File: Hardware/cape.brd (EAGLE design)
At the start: 118.2 x 103.5 mm, 40 parts, among them IC2 74VHC541, IC4 74VHC541, IC5 74VHC541, J1 FCI-10118064-5001310LF, J2 FCI-10118064-5001310LF, J3 RJ45-8P8C, Q2 N-MOSFET-DUALSO8, Q3 N-MOSFET-DUALSO8, Q4 N-MOSFET-DUALSO8, Q5 N-MOSFET-DUALSO8, Q6 N-MOSFET-DUALSO8, Q7 N-MOSFET-DUALSO8, Q8 N-MOSFET-DUALSO8, Q9 N-MOSFET-DUALSO8

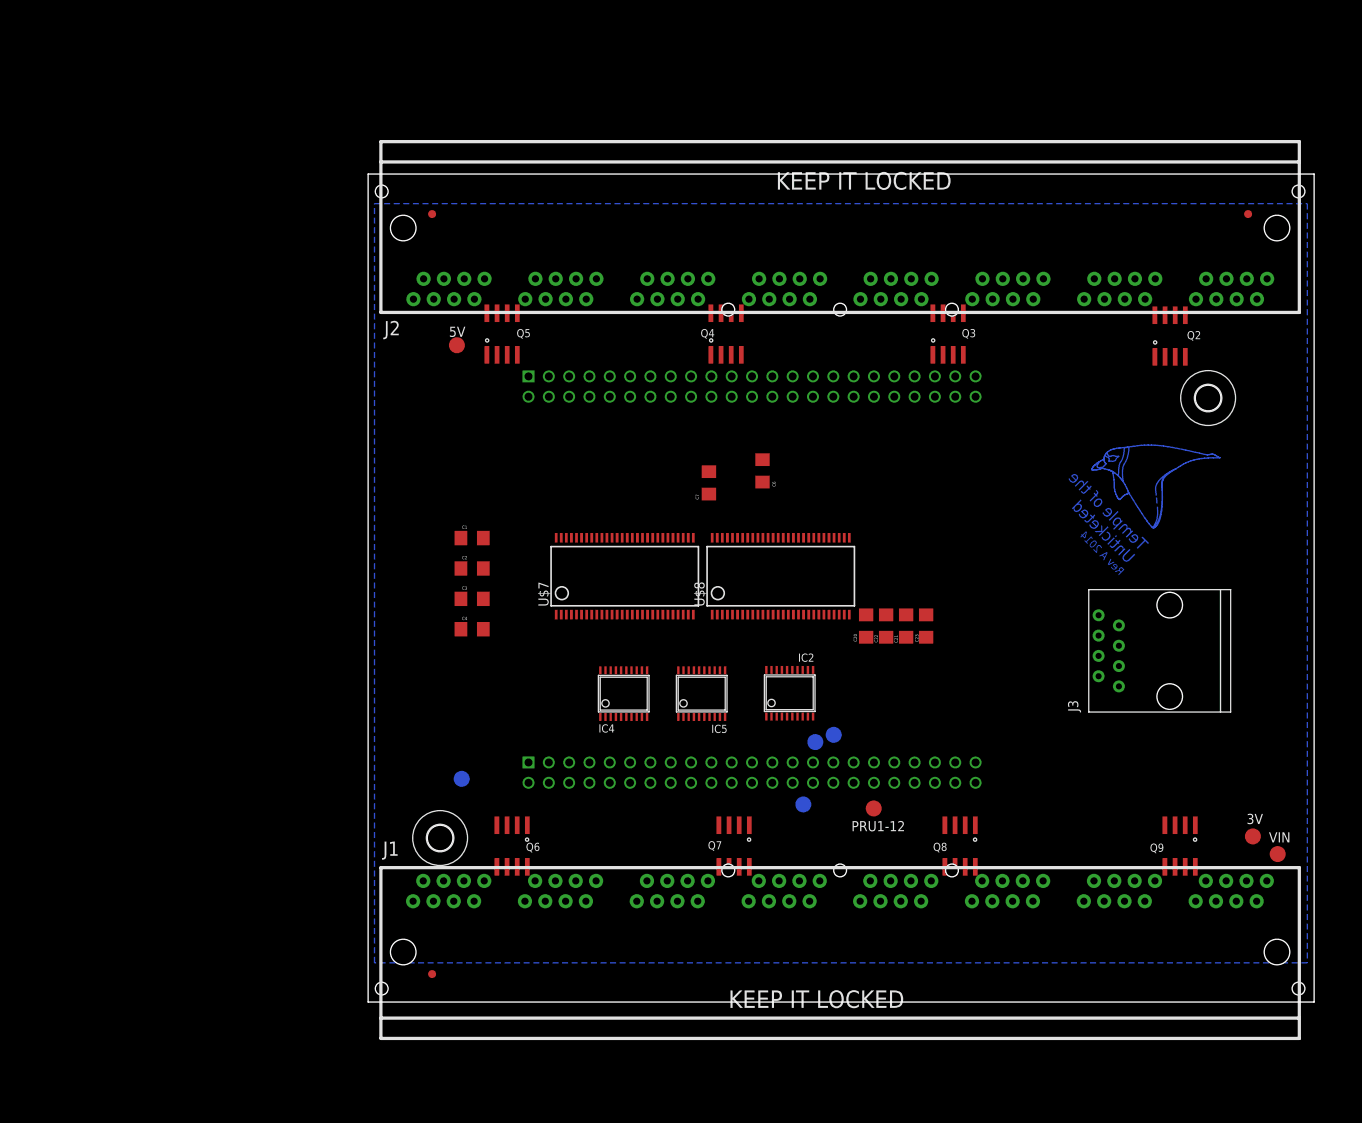
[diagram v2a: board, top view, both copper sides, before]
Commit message: Work on routing A/B and mosfets
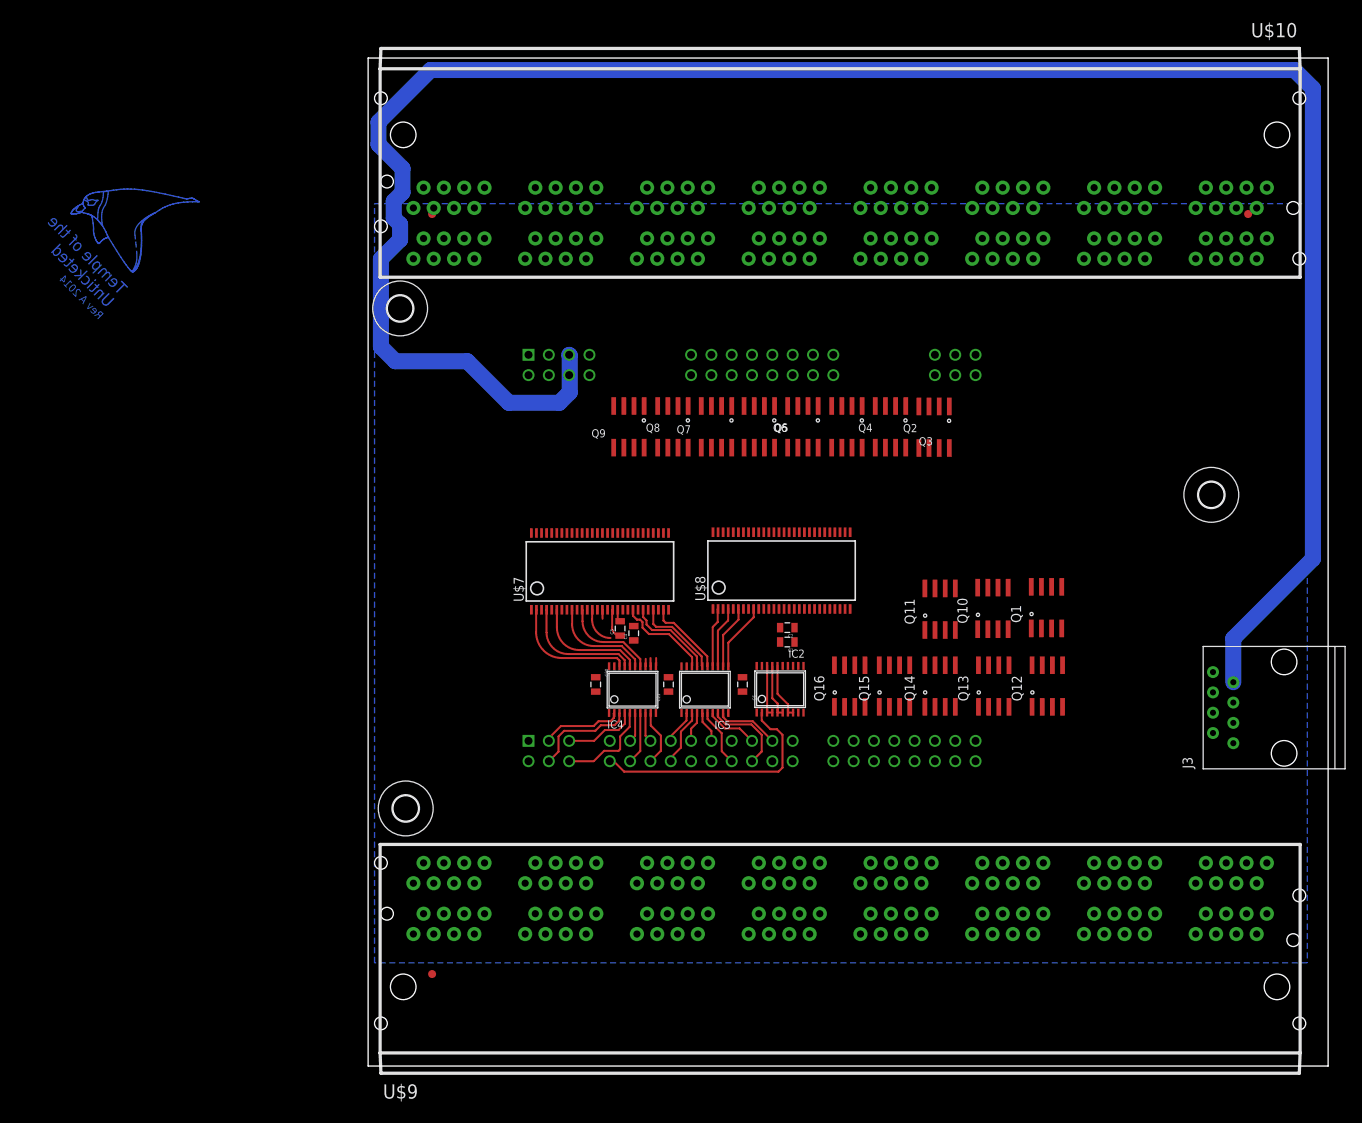
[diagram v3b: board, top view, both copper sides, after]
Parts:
- removed 3V, 5V, GND, PRU1-10, PRU1-12, PRU1-8, PRU1-9, VIN: PTR1TP20R, tenna_avr_AD7021_v0_9_shrink:TP20R
- removed C22, C23, C7: 10uF, SparkFun-Capacitors:1206
- removed J1, J2: FCI-10118064-5001310LF, cape:FCI-10118064-5001310LF
- added Q1, Q10, Q11, Q12, Q13, Q14, Q15, Q16: N-MOSFET-DUALSO8, cape:SO8
- added U$10, U$9: RJ45-8P8C-16FCI-16, cape:FCI-10118074-500A010LF
- added U$12: (no value), holes:3,2
- C1, C2, C20, C21, C3, C4, C6: device SparkFun-Capacitors:1206 -> SparkFun-Capacitors:0805
- moved Q9 86.6 mm to (32.6, 71.9)
- moved Q8 63.5 mm to (38.1, 71.9)
- moved Q6 60.8 mm to (48.9, 71.9)
- moved Q7 52.4 mm to (43.5, 71.9)
- moved C1 41.5 mm to (52.4, 45.0), turned to 180 degrees
- moved C2 40.1 mm to (52.4, 46.8), turned to 180 degrees
- moved Q5 39.3 mm to (54.4, 71.9), turned to 180 degrees
- moved C20 34.6 mm to (28.4, 39.7), turned to 270 degrees
- moved Q2 31.6 mm to (70.8, 71.8), turned to 180 degrees
- moved C21 30.6 mm to (37.5, 39.7)
- moved C6 26.8 mm to (46.8, 39.7)
- moved C4 20.2 mm to (33.2, 46.1), turned to 90 degrees
- moved Q4 19.0 mm to (59.9, 71.9), turned to 180 degrees
- moved C3 18.9 mm to (31.5, 46.7), turned to 90 degrees
- moved J3 16.0 mm to (114.5, 36.8)
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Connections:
- removed net AIN0: U$1.85
- removed net BL0: J1.A6
- removed net BL1: J1.B6
- removed net BL10: J2.C6
- removed net BL11: J2.D6
- removed net BL12: J2.E6
- removed net BL13: J2.F6
- removed net BL14: J2.G6
- removed net BL15: J2.H6
- removed net BL2: J1.C6
- removed net BL3: J1.D6
- removed net BL4: J1.E6
- removed net BL5: J1.F6
- removed net BL6: J1.G6
- removed net BL7: J1.H6
- removed net BL8: J2.A6
- removed net BL9: J2.B6
- removed net DATA0: J1.A1
- removed net DATA1: J1.B1
- removed net DATA10: J2.C1
- removed net DATA11: J2.D1
- removed net DATA12: J2.E1
- removed net DATA13: J2.F1
- removed net DATA14: J2.G1
- removed net DATA15: J2.H1
- removed net DATA2: J1.C1
- removed net DATA3: J1.D1
- removed net DATA4: J1.E1
- removed net DATA5: J1.F1
- removed net DATA6: J1.G1
- removed net DATA7: J1.H1
- removed net DATA8: J2.A1
- removed net DATA9: J2.B1
- removed net DC0: J1.A4, J1.B4, J1.C4, J1.D4
- removed net DC1: J1.E4, J1.F4, J1.G4, J1.H4
- removed net DC2: J2.A4, J2.B4, J2.C4, J2.D4
- removed net DC3: J2.E4, J2.F4, J2.G4, J2.H4
- removed net N$1: Q6.7, Q6.8
- removed net N$2: Q6.5, Q6.6
- removed net N$29: Q9.7, Q9.8
- removed net N$3: Q7.7, Q7.8
- removed net N$30: Q9.5, Q9.6
- removed net N$31: Q2.7, Q2.8
- removed net N$34: Q2.5, Q2.6
- removed net N$35: Q3.7, Q3.8
- removed net N$36: Q3.5, Q3.6
- removed net N$37: Q4.7, Q4.8
- removed net N$38: Q4.5, Q4.6
- removed net N$39: Q5.7, Q5.8
- removed net N$4: Q7.5, Q7.6
- removed net N$40: Q5.5, Q5.6
- removed net N$7: Q8.7, Q8.8
- removed net N$8: Q8.5, Q8.6
- removed net PRU0-0: Q2.2, U$1.77
- removed net PRU0-1: Q2.4, U$1.75
- removed net PRU0-2: Q3.2, U$1.76
- removed net PRU0-3: Q3.4, U$1.74
- removed net PRU0-4: Q4.2, U$1.88
- removed net PRU0-5: Q4.4, U$1.73
- removed net PRU0-6: Q5.2, U$1.87
- removed net PRU0-7: Q5.4, U$1.71
- removed net PRU1-0: Q6.2, U$1.45
- removed net PRU1-1: Q6.4, U$1.46
- removed net PRU1-10: PRU1-10.TP, U$1.28
- removed net PRU1-12: PRU1-12.TP, U$1.21
- removed net PRU1-2: Q7.2, U$1.43
- removed net PRU1-3: Q7.4, U$1.44
- removed net PRU1-4: Q8.2, U$1.41
- removed net PRU1-5: Q8.4, U$1.42
- removed net PRU1-6: Q9.2, U$1.39
- removed net PRU1-7: Q9.4, U$1.40
- removed net PRU1-8: PRU1-8.TP, U$1.27
- removed net PRU1-9: PRU1-9.TP, U$1.29
- removed net SCK0: J1.A8, J1.B8, J1.C8, J1.D8
- removed net SCK1: J1.E8, J1.F8, J1.G8, J1.H8
- removed net SCK2: J2.A8, J2.B8, J2.C8, J2.D8
- removed net SCK3: J2.E8, J2.F8, J2.G8, J2.H8
- removed net VIN: VIN.TP
- new net BL-0-1: Q2.7, Q2.8, U$10.UA6
- new net BL-0-2: Q2.5, Q2.6, U$10.LA6
- new net BL-1-1: Q3.7, Q3.8, U$10.UB6
- new net BL-1-2: Q3.5, Q3.6, U$10.LB6
- new net BL-10-1: U$9.LH6
- new net BL-10-2: U$9.UH6
- new net BL-11-1: Q7.7, Q7.8, U$10.UF6
- new net BL-11-2: Q7.5, Q7.6, U$10.LF6
- new net BL-12-2: U$9.UF6
- new net BL-13-1: U$9.LE6
- new net BL-13-2: U$9.UE6
- new net BL-14-1: Q8.7, Q8.8, U$10.UG6
- new net BL-14-2: Q8.5, Q8.6, U$10.LG6
- new net BL-15-1: Q9.7, Q9.8, U$10.UH6
- new net BL-15-2: Q9.5, Q9.6, U$10.LH6
- new net BL-2-1: U$9.LC6
- new net BL-2-2: U$9.UC6
- new net BL-3-1: U$9.LD6
- new net BL-3-2: U$9.UD6
- new net BL-4-1: Q4.7, Q4.8, U$10.UC6
- new net BL-4-2: Q4.5, Q4.6, U$10.LC6
- new net BL-5-1: Q5.7, Q5.8, U$10.UD6
- new net BL-5-2: Q5.5, Q5.6, U$10.LD6
- new net BL-6-1: U$9.LA6
- new net BL-6-2: U$9.UA6
- new net BL-7-1: U$9.LB6
- new net BL-7-2: U$9.UB6
- new net BL-8-1: Q6.7, Q6.8, U$10.UE6
- new net BL-8-2: Q6.5, Q6.6, U$10.LE6
- new net BL-9-1: U$9.LG6
- new net BL-9-2: U$9.UG6
- new net DATA-0-1: U$10.UA1, U$8.47
- new net DATA-0-2: U$10.LA1, U$8.46
- new net DATA-1-1: U$10.UB1, U$8.50
- new net DATA-1-2: U$10.LB1, U$8.48
- new net DATA-10-1: U$7.39, U$9.LH1
- new net DATA-10-2: U$7.37, U$9.UH1
- new net DATA-11-1: U$10.UF1, U$7.32
- new net DATA-11-2: U$10.LF1, U$7.31
- new net DATA-12-1: U$7.43, U$9.LF1
- new net DATA-12-2: U$7.42, U$9.UF1
- new net DATA-13-1: U$7.45, U$9.LE1
- new net DATA-13-2: U$7.44, U$9.UE1
- new net DATA-14-1: U$10.UG1, U$7.34
- new net DATA-14-2: U$10.LG1, U$7.33
- new net DATA-15-1: U$10.UH1, U$7.36
- new net DATA-15-2: U$10.LH1, U$7.35
- new net DATA-2-1: U$7.50, U$9.LC1
- new net DATA-2-2: U$7.48, U$9.UC1
- new net DATA-3-1: U$7.47, U$9.LD1
- new net DATA-3-2: U$7.46, U$9.UD1
- new net DATA-4-1: U$10.UC1, U$8.52
- new net DATA-4-2: U$10.LC1, U$8.51
- new net DATA-5-1: U$10.UD1, U$8.54
- new net DATA-5-2: U$10.LD1, U$8.53
- new net DATA-6-1: U$7.54, U$9.LA1
- new net DATA-6-2: U$7.53, U$9.UA1
- new net DATA-7-1: U$7.52, U$9.LB1
- new net DATA-7-2: U$7.51, U$9.UB1
- new net DATA-8-1: U$10.UE1, U$7.30
- new net DATA-8-2: U$10.LE1, U$7.29
- new net DATA-9-1: U$7.41, U$9.LG1
- new net DATA-9-2: U$7.40, U$9.UG1
- new net DC: U$10.LA4, U$10.LB4, U$10.LC4, U$10.LD4, U$10.LE4, U$10.LF4, U$10.LG4, U$10.LH4, U$10.UA4, U$10.UB4, U$10.UC4, U$10.UD4, U$10.UE4, U$10.UF4, U$10.UG4, U$10.UH4, U$9.LA4, U$9.LB4, U$9.LC4, U$9.LD4, U$9.LE4, U$9.LF4, U$9.LG4, U$9.LH4, U$9.UA4, U$9.UB4, U$9.UC4, U$9.UD4, U$9.UE4, U$9.UF4, U$9.UG4, U$9.UH4
- new net MUX_S: U$1.28, U$7.1, U$8.1
- new net N$10: Q14.5, Q14.6
- new net N$11: Q15.7, Q15.8
- new net N$12: Q15.5, Q15.6
- new net N$13: Q16.7, Q16.8
- new net N$14: Q16.5, Q16.6
- new net N$15: Q1.7, Q1.8
- new net N$16: Q1.5, Q1.6
- new net N$17: Q10.7, Q10.8
- new net N$18: Q10.5, Q10.6
- new net N$19: Q11.7, Q11.8
- new net N$20: Q11.5, Q11.6
- new net N$21: Q12.7, Q12.8
- new net N$22: U$9.LF6
- new net N$23: Q12.5, Q12.6
- new net N$5: Q13.7, Q13.8
- new net N$6: Q13.5, Q13.6
- new net N$9: Q14.7, Q14.8
- new net PWM0: Q2.2, U$1.87
- new net PWM1: Q2.4, U$1.88
- new net PWM10: Q7.2, U$1.69
- new net PWM11: Q7.4, U$1.68
- new net PWM12: Q8.2, U$1.67
- new net PWM13: Q8.4, U$1.66
- new net PWM14: Q9.2, U$1.65
- new net PWM15: Q9.4, U$1.64
- new net PWM16: Q1.2, U$1.45
- new net PWM17: Q1.4, U$1.46
- new net PWM18: Q10.2, U$1.43
- new net PWM19: Q10.4, U$1.44
- new net PWM2: Q3.2, U$1.77
- new net PWM20: Q11.2, U$1.41
- new net PWM21: Q11.4, U$1.42
- new net PWM22: Q12.2, U$1.39
- new net PWM23: Q12.4, U$1.40
- new net PWM24: Q13.2, U$1.37
- new net PWM25: Q13.4, U$1.38
- new net PWM26: Q14.2, U$1.35
- new net PWM27: Q14.4, U$1.36
- new net PWM28: Q15.2, U$1.33
- new net PWM29: Q15.4, U$1.34
- new net PWM3: Q3.4, U$1.76
- new net PWM30: Q16.2, U$1.31
- new net PWM31: Q16.4, U$1.32
- new net PWM4: Q4.2, U$1.75
- new net PWM5: Q4.4, U$1.74
- new net PWM6: Q5.2, U$1.73
- new net PWM7: Q5.4, U$1.72
- new net PWM8: Q6.2, U$1.71
- new net PWM9: Q6.4, U$1.70
- new net SCL-A-1: U$8.45, U$9.LA8, U$9.LB8
- new net SCL-A-2: U$8.44, U$9.UA8, U$9.UB8
- new net SCL-B-1: U$8.43, U$9.LC8, U$9.LD8
- new net SCL-B-2: U$8.42, U$9.UC8, U$9.UD8
- new net SCL-C-1: U$8.41, U$9.LE8, U$9.LF8
- new net SCL-C-2: U$8.40, U$9.UE8, U$9.UF8
- new net SCL-D-1: U$8.39, U$9.LG8, U$9.LH8
- new net SCL-D-2: U$8.37, U$9.UG8, U$9.UH8
- new net SCL-E-1: U$10.UG8, U$10.UH8, U$8.36
- new net SCL-E-2: U$10.LG8, U$10.LH8, U$8.35
- new net SCL-F-1: U$10.UE8, U$10.UF8, U$8.34
- new net SCL-F-2: U$10.LE8, U$10.LF8, U$8.33
- new net SCL-G-1: U$10.UC8, U$10.UD8, U$8.32
- new net SCL-G-2: U$10.LC8, U$10.LD8, U$8.31
- new net SCL-H-1: U$10.UA8, U$10.UB8, U$8.30
- new net SCL-H-2: U$10.LA8, U$10.LB8, U$8.29
- net GND: now also J3.2, J3.4, J3.6, J3.8, Q1.1, Q1.3, Q10.1, Q10.3, Q11.1, Q11.3, Q12.1, Q12.3, Q13.1, Q13.3, Q14.1, Q14.3, Q15.1, Q15.3, Q16.1, Q16.3, U$10.LA2, U$10.LA7, U$10.LB2, U$10.LB7, U$10.LC2, U$10.LC7, U$10.LD2, U$10.LD7, U$10.LE2, U$10.LE7, U$10.LF2, U$10.LF7, U$10.LG2, U$10.LG7, U$10.LH2, U$10.LH7, U$10.UA2, U$10.UA7, U$10.UB2, U$10.UB7, U$10.UC2, U$10.UC7, U$10.UD2, U$10.UD7, U$10.UE2, U$10.UE7, U$10.UF2, U$10.UF7, U$10.UG2, U$10.UG7, U$10.UH2, U$10.UH7, U$9.LA2, U$9.LA7, U$9.LB2, U$9.LB7, U$9.LC2, U$9.LC7, U$9.LD2, U$9.LD7, U$9.LE2, U$9.LE7, U$9.LF2, U$9.LF7, U$9.LG2, U$9.LG7, U$9.LH2, U$9.LH7, U$9.UA2, U$9.UA7, U$9.UB2, U$9.UB7, U$9.UC2, U$9.UC7, U$9.UD2, U$9.UD7, U$9.UE2, U$9.UE7, U$9.UF2, U$9.UF7, U$9.UG2, U$9.UG7, U$9.UH2, U$9.UH7; no longer C22.2, C23.2, C7.2, GND.TP, J1.A2, J1.A7, J1.B2, J1.B7, J1.C2, J1.C7, J1.D2, J1.D7, J1.E2, J1.E7, J1.F2, J1.F7, J1.G2, J1.G7, J1.H2, J1.H7, J2.A2, J2.A7, J2.B2, J2.B7, J2.C2, J2.C7, J2.D2, J2.D7, J2.E2, J2.E7, J2.F2, J2.F7, J2.G2, J2.G7, J2.H2, J2.H7, J3.1, J3.3, J3.5, J3.7
- net RST: now also U$10.LA5, U$10.LB5, U$10.LC5, U$10.LD5, U$10.LE5, U$10.LF5, U$10.LG5, U$10.LH5, U$10.UA5, U$10.UB5, U$10.UC5, U$10.UD5, U$10.UE5, U$10.UF5, U$10.UG5, U$10.UH5, U$9.LA5, U$9.LB5, U$9.LC5, U$9.LD5, U$9.LE5, U$9.LF5, U$9.LG5, U$9.LH5, U$9.UA5, U$9.UB5, U$9.UC5, U$9.UD5, U$9.UE5, U$9.UF5, U$9.UG5, U$9.UH5; no longer J1.A5, J1.B5, J1.C5, J1.D5, J1.E5, J1.F5, J1.G5, J1.H5, J2.A5, J2.B5, J2.C5, J2.D5, J2.E5, J2.F5, J2.G5, J2.H5
- net VCC3V3: now also U$10.LA3, U$10.LB3, U$10.LC3, U$10.LD3, U$10.LE3, U$10.LF3, U$10.LG3, U$10.LH3, U$10.UA3, U$10.UB3, U$10.UC3, U$10.UD3, U$10.UE3, U$10.UF3, U$10.UG3, U$10.UH3, U$9.LA3, U$9.LB3, U$9.LC3, U$9.LD3, U$9.LE3, U$9.LF3, U$9.LG3, U$9.LH3, U$9.UA3, U$9.UB3, U$9.UC3, U$9.UD3, U$9.UE3, U$9.UF3, U$9.UG3, U$9.UH3; no longer 3V.TP, C22.1, C23.1, C7.1, J1.A3, J1.B3, J1.C3, J1.D3, J1.E3, J1.F3, J1.G3, J1.H3, J2.A3, J2.B3, J2.C3, J2.D3, J2.E3, J2.F3, J2.G3, J2.H3
- net VCC5V: now also J3.1, J3.3, J3.5, J3.7; no longer 5V.TP, J3.2, J3.4, J3.6, J3.8
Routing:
- net VCC5V: track 0.00 -> 265.4 mm
- net SCL_RAW: track 0.00 -> 30.8 mm
- net 1A: track 0.00 -> 15.5 mm
- net 2A: track 0.00 -> 14.8 mm
- net 3A: track 0.00 -> 13.8 mm
- net AD7: track 0.00 -> 13.0 mm
- net 4A: track 0.00 -> 12.4 mm
- net AD3: track 0.00 -> 12.0 mm
- net 9A: track 0.00 -> 11.8 mm
- net 5A: track 0.00 -> 11.5 mm
- net 10A: track 0.00 -> 11.2 mm
- net 11A: track 0.00 -> 10.8 mm
- net AD1: track 0.00 -> 10.7 mm
- net AD6: track 0.00 -> 10.2 mm
- net 12A: track 0.00 -> 9.93 mm
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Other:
- board size 118.2 x 103.5 mm -> 120 x 126 mm

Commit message: More routing
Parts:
- moved U$2 9.82 mm to (-5.10, 24.8)
- moved Q10 6.82 mm to (84.4, 51.8)
- moved Q1 6.82 mm to (91.1, 51.9)
- moved Q11 6.82 mm to (77.8, 51.7)
- moved Q12 6.82 mm to (91.2, 42.1)
- moved Q13 6.82 mm to (84.5, 42.1)
- moved Q14 6.82 mm to (77.8, 42.1)
- moved Q15 6.82 mm to (72.1, 42.1)
- moved Q16 6.82 mm to (66.5, 42.1)
- moved J3 5.60 mm to (114.5, 42.4)
- moved U$7 2.00 mm to (28.8, 56.2)
- moved C3 1.90 mm to (31.4, 48.6), turned to 0 degrees
- moved C20 1.00 mm to (28.6, 40.7)
- moved C4 1.00 mm to (32.4, 46.7), turned to 0 degrees
- moved C21 1.00 mm to (37.5, 40.7)
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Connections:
- removed net N$10: Q14.5, Q14.6
- removed net N$11: Q15.7, Q15.8
- removed net N$12: Q15.5, Q15.6
- removed net N$13: Q16.7, Q16.8
- removed net N$14: Q16.5, Q16.6
- removed net N$15: Q1.7, Q1.8
- removed net N$16: Q1.5, Q1.6
- removed net N$17: Q10.7, Q10.8
- removed net N$18: Q10.5, Q10.6
- removed net N$19: Q11.7, Q11.8
- removed net N$20: Q11.5, Q11.6
- removed net N$21: Q12.7, Q12.8
- removed net N$22: U$9.LF6
- removed net N$23: Q12.5, Q12.6
- removed net N$5: Q13.7, Q13.8
- removed net N$6: Q13.5, Q13.6
- removed net N$9: Q14.7, Q14.8
- new net BL-12-1: Q14.5, Q14.6, U$9.LF6
- net BL-10-1: now also Q16.5, Q16.6
- net BL-10-2: now also Q16.7, Q16.8
- net BL-12-2: now also Q14.7, Q14.8
- net BL-13-1: now also Q12.5, Q12.6
- net BL-13-2: now also Q12.7, Q12.8
- net BL-2-1: now also Q11.7, Q11.8
- net BL-2-2: now also Q11.5, Q11.6
- net BL-3-1: now also Q13.5, Q13.6
- net BL-3-2: now also Q13.7, Q13.8
- net BL-6-1: now also Q1.7, Q1.8
- net BL-6-2: now also Q1.5, Q1.6
- net BL-7-1: now also Q10.7, Q10.8
- net BL-7-2: now also Q10.5, Q10.6
- net BL-9-1: now also Q15.5, Q15.6
- net BL-9-2: now also Q15.7, Q15.8
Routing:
- net BL-6-2: track 0.00 -> 196.7 mm, vias 0 -> 1
- net BL-6-1: track 0.00 -> 193.0 mm
- net BL-7-2: track 0.00 -> 188.4 mm, vias 0 -> 2
- net BL-7-1: track 0.00 -> 180.1 mm, vias 0 -> 2
- net RST: track 0.00 -> 175.3 mm, vias 0 -> 6
- net BL-2-2: track 0.00 -> 175.1 mm, vias 0 -> 3
- net BL-2-1: track 0.00 -> 166.9 mm, vias 0 -> 2
- net DATA-10-1: track 0.00 -> 156.9 mm, vias 0 -> 2
- net DATA-10-2: track 0.00 -> 156.3 mm
- net BL-3-2: track 0.00 -> 148.2 mm, vias 0 -> 2
- net DATA-9-1: track 0.00 -> 143.3 mm
- net DATA-9-2: track 0.00 -> 143.3 mm
- net SCL-D-2: track 0.00 -> 134.2 mm
- net BL-3-1: track 0.00 -> 134.1 mm, vias 0 -> 2
- net DATA-12-1: track 0.00 -> 131.7 mm
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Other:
- board size 120 x 126 mm -> 123 x 126 mm
